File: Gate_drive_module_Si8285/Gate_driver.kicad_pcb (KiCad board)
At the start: 2 copper layers, 90 x 50 mm, 39 parts, among them J1 CONN_01X10, J2 CONN_01X04, J3 CONN_01X03, J4 CONN_01X03, J5 CONN_01X03, U1 Si8285, U2 Mornsun_QA01C

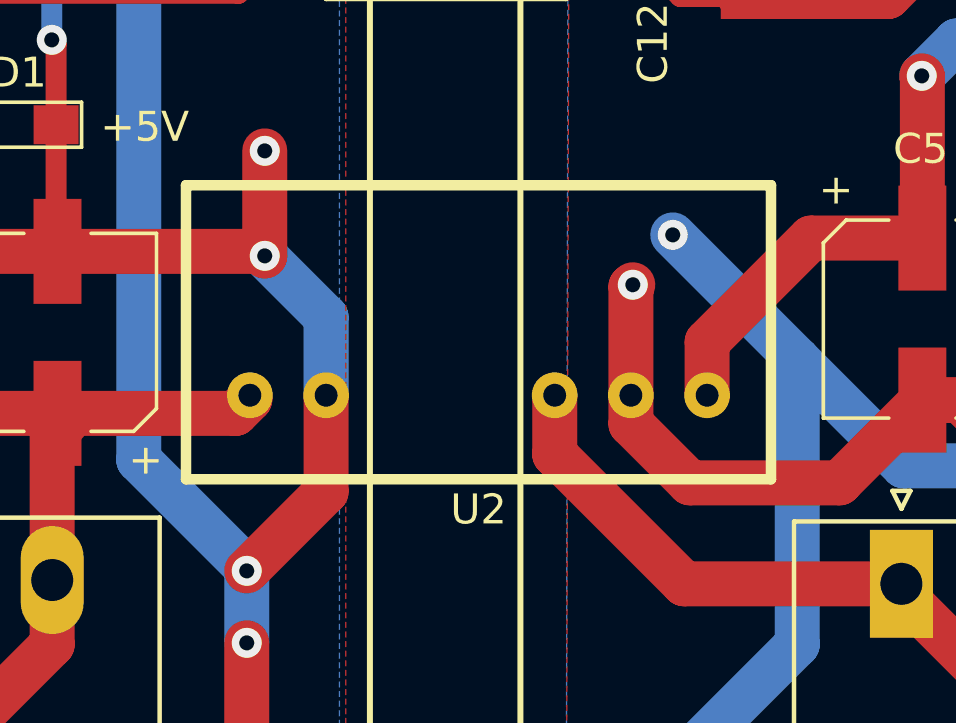
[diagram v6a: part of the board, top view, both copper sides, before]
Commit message: Replaced DC/DC converter footprint for increased pad size
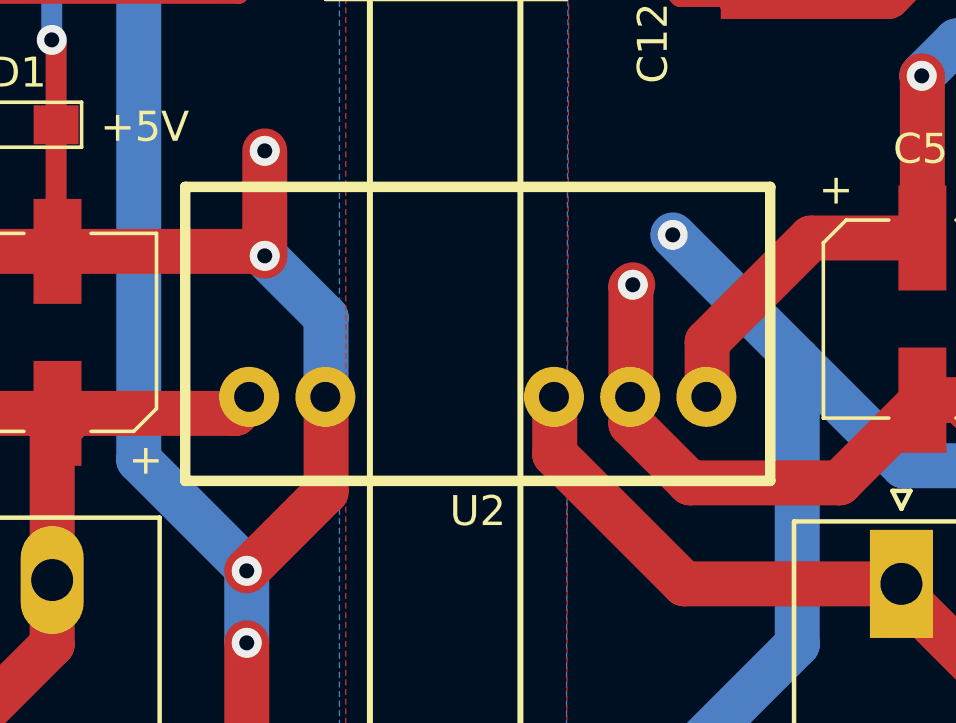
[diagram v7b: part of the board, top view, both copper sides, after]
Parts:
- moved U2 0.06 mm to (136.5, 139.5)
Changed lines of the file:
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@@
     (links 70)
     (no_connects 0)
-    (area 84.450001 94.6 203.43 163.500001)
+    (area 94.949999 105.949999 185.050001 156.050001)
     (thickness 1.6)
     (drawings 40)
@@
     )
   )
-  (module Mornsun:QA01C (layer F.Cu)
-    (at 136.525 139.446)
-    (fp_text reference U2 (at 0 3.81) (layer F.SilkS)
-      (effects (font (size 1 1) (thickness 0.15)))
-    )
-    (fp_text value Mornsun_QA01C (at 0 -5.08) (layer F.Fab)
-      (effects (font (size 1 1) (thickness 0.15)))
-    )
-    (fp_line (start -9.75 -7) (end 9.75 -7) (layer F.SilkS) (width 0.35))
-    (fp_line (start 9.75 2.8) (end 9.75 -7) (layer F.SilkS) (width 0.35))
-    (fp_line (start 9.75 2.8) (end -9.75 2.8) (layer F.SilkS) (width 0.35))
-    (fp_line (start -9.75 2.8) (end -9.75 -7) (layer F.SilkS) (width 0.35))
-    (pad 1 thru_hole circle (at -7.62 0) (size 1.524 1.524) (drill 0.762) (layers *.Cu *.Mask)
-      (net 3 +15V))
-    (pad 2 thru_hole circle (at -5.08 0) (size 1.524 1.524) (drill 0.762) (layers *.Cu *.Mask)
-      (net 2 GND))
-    (pad 5 thru_hole circle (at 2.54 0) (size 1.524 1.524) (drill 0.762) (layers *.Cu *.Mask)
-      (net 16 VEE_ISO))
-    (pad 6 thru_hole circle (at 5.08 0) (size 1.524 1.524) (drill 0.762) (layers *.Cu *.Mask)
-      (net 15 GND_ISO))
-    (pad 7 thru_hole circle (at 7.62 0) (size 1.524 1.524) (drill 0.762) (layers *.Cu *.Mask)
-      (net 14 VCC_ISO))
-    (model ${SWITCHCRAFTLIB}/packages3d/mornsun.3dshapes/QA01c.wrl
-      (at (xyz 0 0 0))
-      (scale (xyz 1 1 1))
-      (rotate (xyz 0 0 0))
-    )
-  )
   (module Mounting_Holes:MountingHole_3.2mm_M3_ISO7380_Pad (layer F.Cu)
     (at 100 110)
@@
       (xy -0.113933 -2.757629) (xy -0.013056 -2.757714) (xy 0 -2.757714) (xy 0.10391 -2.757652)) (layer F.SilkS) (width 0.01))
   )
+  (module Mornsun:QA01C (layer F.Cu)
+    (at 136.5 139.5)
+    (fp_text reference U2 (at 0 3.81) (layer F.SilkS)
+      (effects (font (size 1 1) (thickness 0.15)))
+    )
+    (fp_text value Mornsun_QA01C (at 0 -5.08) (layer F.Fab)
+      (effects (font (size 1 1) (thickness 0.15)))
+    )
+    (fp_line (start -9.75 -7) (end 9.75 -7) (layer F.SilkS) (width 0.35))
+    (fp_line (start 9.75 2.8) (end 9.75 -7) (layer F.SilkS) (width 0.35))
+    (fp_line (start 9.75 2.8) (end -9.75 2.8) (layer F.SilkS) (width 0.35))
+    (fp_line (start -9.75 2.8) (end -9.75 -7) (layer F.SilkS) (width 0.35))
+    (pad 1 thru_hole circle (at -7.62 0) (size 2 2) (drill 1) (layers *.Cu *.Mask)
+      (net 3 +15V))
+    (pad 2 thru_hole circle (at -5.08 0) (size 2 2) (drill 1) (layers *.Cu *.Mask)
+      (net 2 GND))
+    (pad 5 thru_hole circle (at 2.54 0) (size 2 2) (drill 1) (layers *.Cu *.Mask)
+      (net 16 VEE_ISO))
+    (pad 6 thru_hole circle (at 5.08 0) (size 2 2) (drill 1) (layers *.Cu *.Mask)
+      (net 15 GND_ISO))
+    (pad 7 thru_hole circle (at 7.62 0) (size 2 2) (drill 1) (layers *.Cu *.Mask)
+      (net 14 VCC_ISO))
+    (model ${SWITCHCRAFTLIB}/packages3d/mornsun.3dshapes/QA01c.wrl
+      (at (xyz 0 0 0))
+      (scale (xyz 1 1 1))
+      (rotate (xyz 0 0 0))
+    )
+  )
   (gr_text SOURCE (at 180.75 138.5) (layer B.SilkS)
